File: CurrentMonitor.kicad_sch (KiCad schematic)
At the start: 33 parts, among them J1 USB_B_Micro, J10 Screw_Terminal_01x02, J11 Barrel_Jack_Switch_SMT, J12 Conn_01x05, J13 Conn_01x05, J14 USB_A, J15 Conn_Coaxial, J2 Conn_01x05, J3 Conn_01x05, J4 Barrel_Jack_Switch_SMT, J5 Screw_Terminal_01x02, J6 Conn_01x02_Socket, J7 Screw_Terminal_01x02, J8 Conn_02x03_Odd_Even, J9 Conn_01x02_Socket

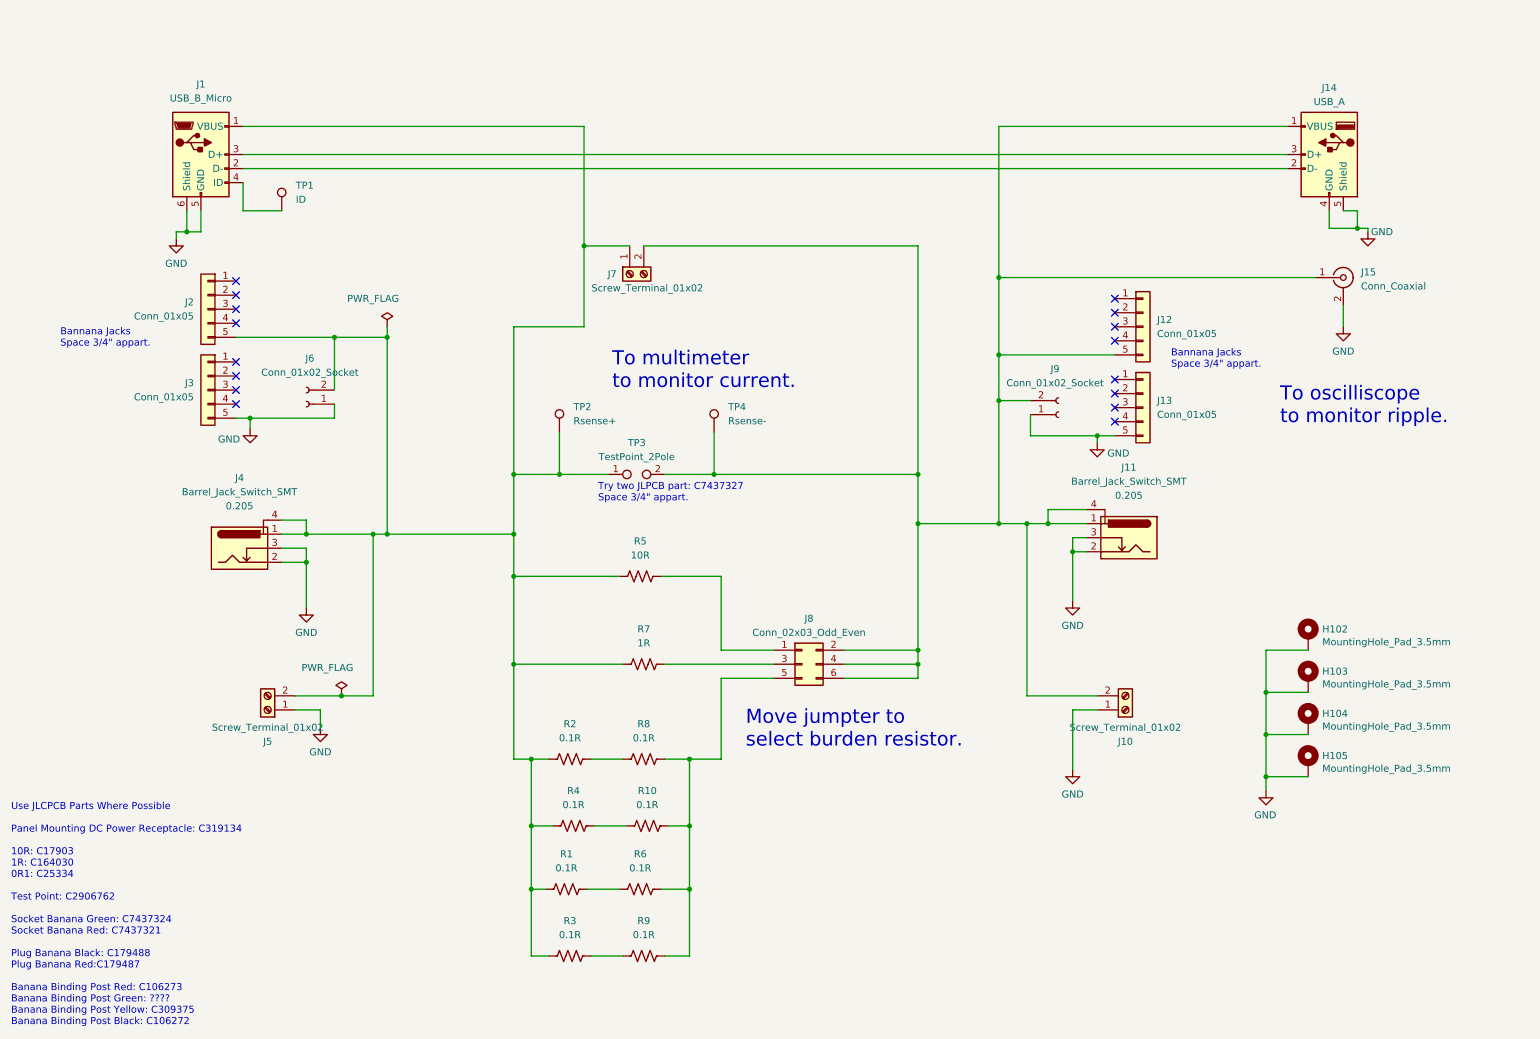
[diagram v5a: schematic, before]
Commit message: Update with USB type A footprint. Update footprint of Barrel jack, mounting holes and bannana jacks. No ERC errors.
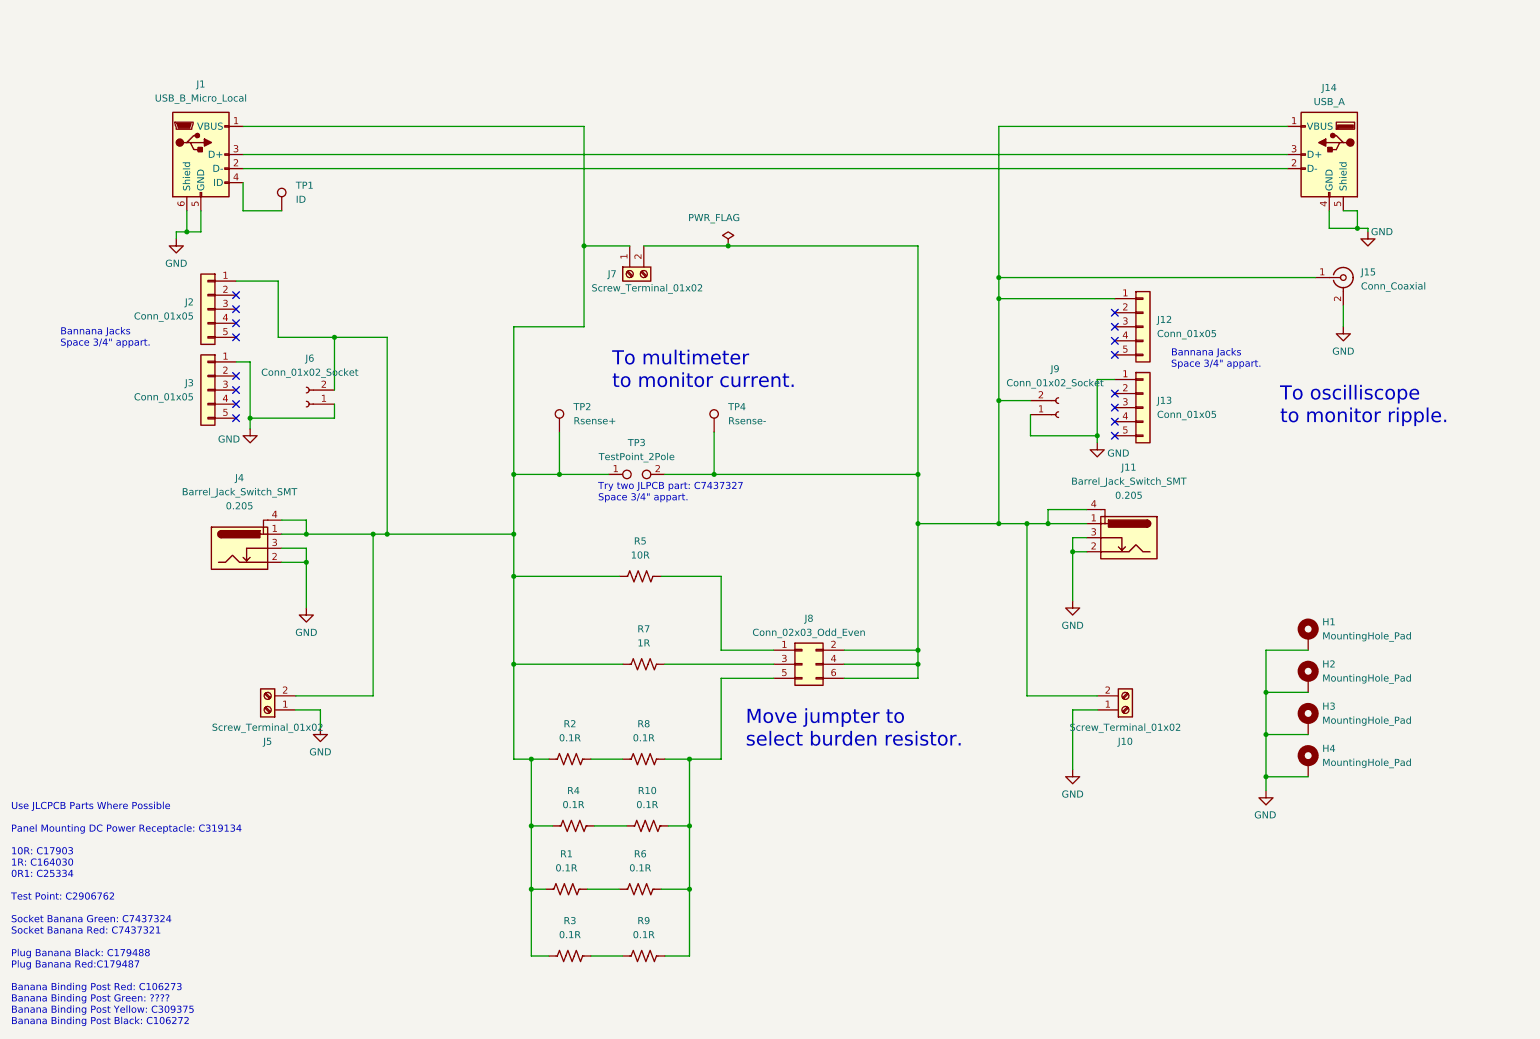
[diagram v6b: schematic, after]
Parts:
- removed H102, H103, H104, H105: MountingHole_Pad_3.5mm, MountingHole:MountingHole_3.5mm_Pad_Via, symbol GPAD_SCH_LIB:MountingHole_Pad_3.5mm
- added H1, H2, H3, H4: MountingHole_Pad, MountingHole:MountingHole_3.5mm_Pad_Via, symbol Mechanical:MountingHole_Pad
- J1: value USB_B_Micro -> USB_B_Micro_Local; footprint (none) -> PubInv_KiCad_PCB:USB_Micro-B_Amphenol_10118194_Horizontal; Cost 0.0329 -> 0.2042; Distributor 1 PN C404969 -> C132563
- J11, J4: footprint Connector_BarrelJack:BarrelJack_CLIFF_FC681465S_SMT_Horizontal -> PubInv_KiCad_PCB:BarrelJack_CLIFF_FC681465S_SMT_Horizontal
- J12, J13, J2, J3: footprint Connector:Banana_Cliff_FCR7350x_S16N-PC_Horizontal -> PubInv_KiCad_PCB:Banana_Cliff_FCR7350x_S16N-PC_Horizontal_5Pins
- J14: footprint (none) -> PubInv_KiCad_PCB:USB_A_JLCPCB_C3038692_Horizontal
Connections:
- net GND: now also J13.1 (Pin_1), J3.1 (Pin_1), H1.1, H2.1, H3.1, H4.1; no longer J13.5 (Pin_5), J3.5 (Pin_5)
- net at J1.1 (VBUS), J4.1, J4.4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: now also J2.1 (Pin_1); no longer J2.5 (Pin_5)
- net at J10.2 (Pin_2), J11.1, J11.4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: now also J12.1 (Pin_1); no longer J12.5 (Pin_5)

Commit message: Route copper on PCB.
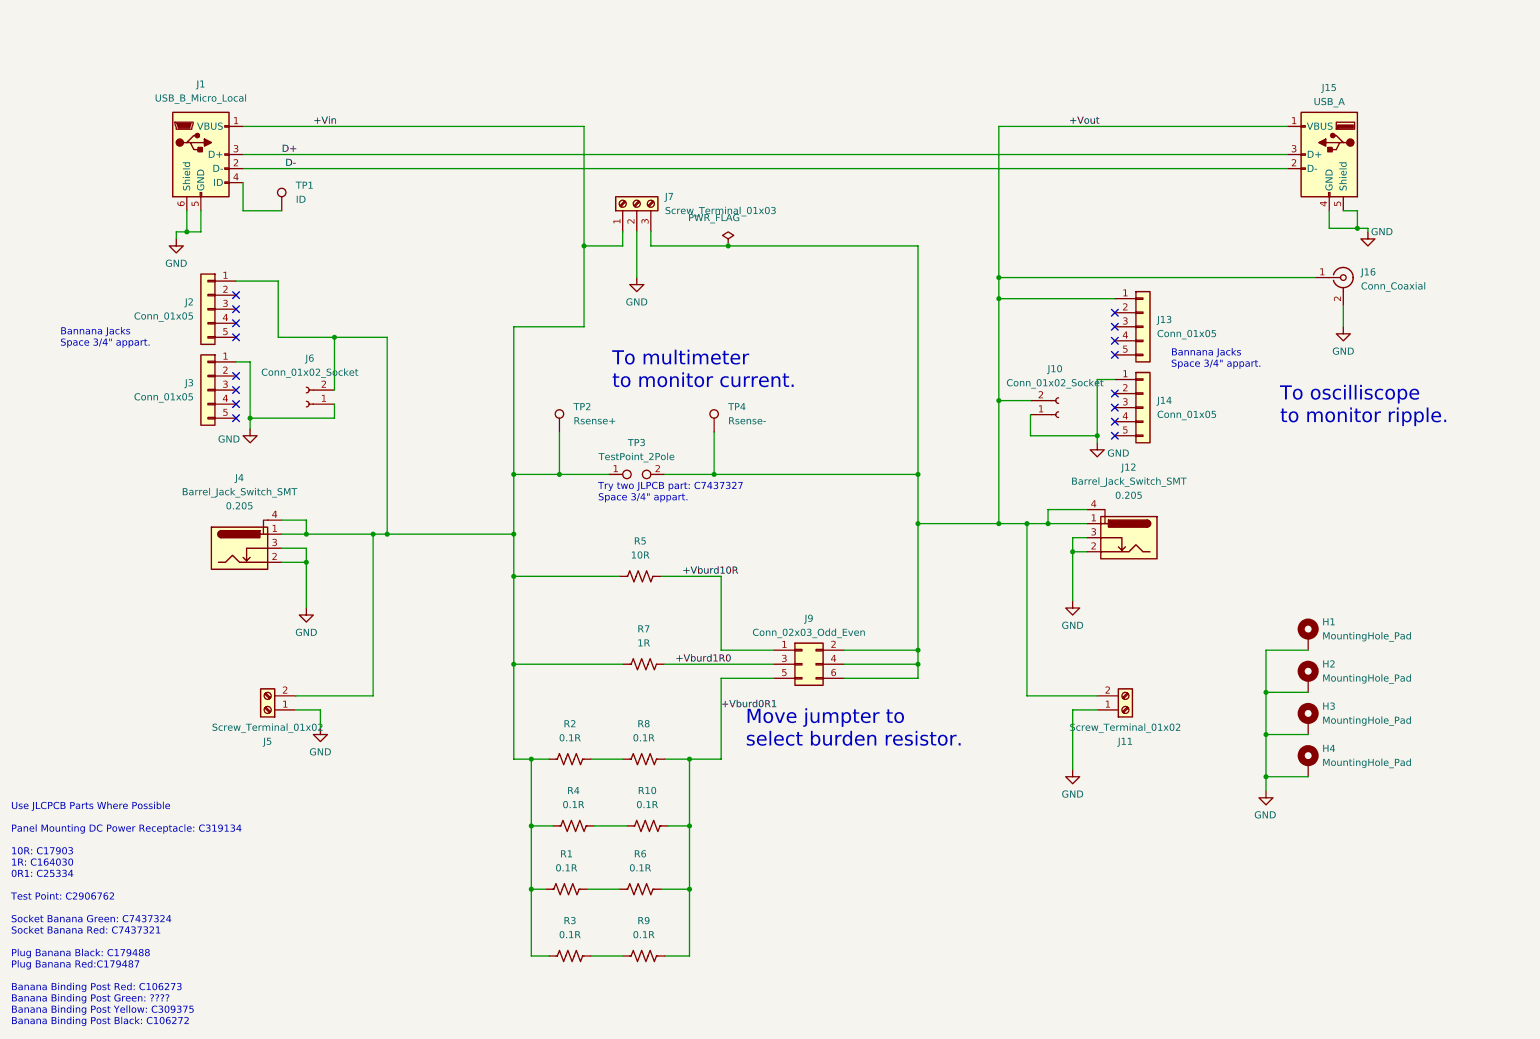
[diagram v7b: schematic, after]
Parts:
- removed J7: Screw_Terminal_01x02, TerminalBlock_Phoenix_MKDS-1,5-2_1x02_P5.00mm_Horizontal, symbol Connector:Screw_Terminal_01x02
- added J7: Screw_Terminal_01x03, TerminalBlock_Phoenix:TerminalBlock_Phoenix_MKDS-1,5-3_1x03_P5.00mm_Horizontal, symbol Connector:Screw_Terminal_01x03
- renumbered J9 to J10, J10 to J11, J11 to J12, J12 to J13, J13 to J14, J14 to J15, J15 to J16, J8 to J9
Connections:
- net GND: now also J7.2 (Pin_2)
- net +Vburd0R1: now reaches J9.5 (Pin_5), R10.2, R6.2, R8.2, R9.2
- net +Vin: now reaches J1.1 (VBUS), J2.1 (Pin_1), J4.1, J4.4, J5.2 (Pin_2), J6.2 (Pin_2), R1.1, R2.1, R3.1, R4.1, R5.1, R7.1, TP2.1, TP3.1
- net +Vin: now also J7.1 (Pin_1)
- net +Vburd1R0: now reaches J9.3 (Pin_3), R7.2
- net D-: now reaches J1.2 (D-), J15.2 (D-)
- net D+: now reaches J1.3 (D+), J15.3 (D+)
- net +Vburd10R: now reaches J9.1 (Pin_1), R5.2
- net +Vout: now reaches J10.2 (Pin_2), J11.2 (Pin_2), J12.1, J12.4, J13.1 (Pin_1), J15.1 (VBUS), J16.1 (In), J9.2 (Pin_2), J9.4 (Pin_4), J9.6 (Pin_6), TP3.2, TP4.1
- net +Vout: now also J7.3 (Pin_3)
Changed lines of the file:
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@@
+    (stroke (width 0) (type default))
+  )
+  (wire (pts (xy 130.81 52.07) (xy 130.81 60.325))
     (stroke (width 0) (type default))
   )
@@
     (stroke (width 0) (type default))
   )
+  (wire (pts (xy 133.35 52.07) (xy 133.35 54.61))
+    (stroke (width 0) (type default))
+  )
   (wire (pts (xy 60.96 75.565) (xy 60.96 85.725))
     (stroke (width 0) (type default))
@@
     (stroke (width 0) (type default))
   )
+  (wire (pts (xy 133.35 54.61) (xy 147.32 54.61))
+    (stroke (width 0) (type default))
+  )
   (wire (pts (xy 108.585 106.68) (xy 108.585 114.3))
     (stroke (width 0) (type default))
@@
     (stroke (width 0) (type default))
   )
-  (wire (pts (xy 129.54 54.61) (xy 121.285 54.61))
-    (stroke (width 0) (type default))
-  )
   (wire (pts (xy 209.55 107.315) (xy 209.55 109.855))
     (stroke (width 0) (type default))
@@
     (stroke (width 0) (type default))
   )
+  (wire (pts (xy 128.27 52.07) (xy 128.27 54.61))
+    (stroke (width 0) (type default))
+  )
   (wire (pts (xy 69.215 135.89) (xy 83.185 135.89))
     (stroke (width 0) (type default))
@@
     (stroke (width 0) (type default))
   )
+  (wire (pts (xy 128.27 54.61) (xy 121.285 54.61))
+    (stroke (width 0) (type default))
+  )
   (wire (pts (xy 196.215 82.55) (xy 201.93 82.55))
     (stroke (width 0) (type default))
@@
   )
   (wire (pts (xy 116.84 95.885) (xy 108.585 95.885))
-    (stroke (width 0) (type default))
-  )
-  (wire (pts (xy 132.08 54.61) (xy 147.32 54.61))
     (stroke (width 0) (type default))
   )
@@
   )
   (text "Bannana Jacks\nSpace 3/4\" appart." (at 227.33 76.835 0)
+    (effects (font (size 1.27 1.27)) (justify left bottom))
+  )
+  (label "D-" (at 67.31 40.64 0) (fields_autoplaced)
+    (effects (font (size 1.27 1.27)) (justify left bottom))
+  )
+  (label "+Vout" (at 208.915 33.02 0) (fields_autoplaced)
+    (effects (font (size 1.27 1.27)) (justify left bottom))
+  )
+  (label "+Vburd10R" (at 139.065 114.3 0) (fields_autoplaced)
+    (effects (font (size 1.27 1.27)) (justify left bottom))
+  )
+  (label "+Vin" (at 72.39 33.02 0) (fields_autoplaced)
+    (effects (font (size 1.27 1.27)) (justify left bottom))
+  )
+  (label "+Vburd1R0" (at 137.795 130.175 0) (fields_autoplaced)
+    (effects (font (size 1.27 1.27)) (justify left bottom))
+  )
+  (label "+Vburd0R1" (at 146.05 138.43 0) (fields_autoplaced)
+    (effects (font (size 1.27 1.27)) (justify left bottom))
+  )
+  (label "D+" (at 66.675 38.1 0) (fields_autoplaced)
     (effects (font (size 1.27 1.27)) (justify left bottom))
   )
@@
   (symbol (lib_id "Connector:USB_A") (at 255.905 38.1 0) (mirror y) (unit 1)
     (in_bom yes) (on_board yes) (dnp no)
-    (property "Reference" "J14" (at 255.905 26.035 0)
+    (property "Reference" "J15" (at 255.905 26.035 0)
       (effects (font (size 1.27 1.27)))
     )
@@
       (project "CurrentMonitor"
         (path "/c2625580-5dc2-4487-938a-c703153fa89f"
-          (reference "J14") (unit 1)
+          (reference "J15") (unit 1)
         )
       )
@@
   (symbol (lib_id "Connector_Generic:Conn_02x03_Odd_Even") (at 160.655 130.175 0) (unit 1)
     (in_bom yes) (on_board yes) (dnp no) (fields_autoplaced)
-    (property "Reference" "J8" (at 161.925 121.92 0)
+    (property "Reference" "J9" (at 161.925 121.92 0)
       (effects (font (size 1.27 1.27)))
     )
@@
       (project "CurrentMonitor"
         (path "/c2625580-5dc2-4487-938a-c703153fa89f"
-          (reference "J8") (unit 1)
+          (reference "J9") (unit 1)
         )
       )
@@
   (symbol (lib_id "Connector:Screw_Terminal_01x02") (at 219.075 138.43 0) (mirror x) (unit 1)
     (in_bom yes) (on_board yes) (dnp no)
-    (property "Reference" "J10" (at 219.075 144.145 0)
+    (property "Reference" "J11" (at 219.075 144.145 0)
       (effects (font (size 1.27 1.27)))
     )
@@
       (project "CurrentMonitor"
         (path "/c2625580-5dc2-4487-938a-c703153fa89f"
-          (reference "J10") (unit 1)
+          (reference "J11") (unit 1)
         )
       )
@@
   (symbol (lib_id "Connector_Generic:Conn_01x05") (at 222.25 69.215 0) (unit 1)
     (in_bom yes) (on_board yes) (dnp no) (fields_autoplaced)
-    (property "Reference" "J12" (at 224.79 67.945 0)
+    (property "Reference" "J13" (at 224.79 67.945 0)
       (effects (font (size 1.27 1.27)) (justify left))
     )
@@
       (project "CurrentMonitor"
         (path "/c2625580-5dc2-4487-938a-c703153fa89f"
-          (reference "J12") (unit 1)
+          (reference "J13") (unit 1)
         )
       )
@@
   (symbol (lib_id "PubInv_KiCad_SCH_LIB:Barrel_Jack_Switch_SMT") (at 219.71 107.315 0) (mirror y) (unit 1)
     (in_bom yes) (on_board yes) (dnp no)
-    (property "Reference" "J11" (at 219.71 94.615 0)
+    (property "Reference" "J12" (at 219.71 94.615 0)
       (effects (font (size 1.27 1.27)))
     )
@@
       (project "CurrentMonitor"
         (path "/c2625580-5dc2-4487-938a-c703153fa89f"
-          (reference "J11") (unit 1)
+          (reference "J12") (unit 1)
         )
       )
@@
   (symbol (lib_id "Connector:Conn_01x02_Socket") (at 207.01 85.09 0) (mirror x) (unit 1)
     (in_bom no) (on_board yes) (dnp no)
-    (property "Reference" "J9" (at 206.375 76.835 0)
+    (property "Reference" "J10" (at 206.375 76.835 0)
       (effects (font (size 1.27 1.27)))
     )
@@
       (project "CurrentMonitor"
         (path "/c2625580-5dc2-4487-938a-c703153fa89f"
-          (reference "J9") (unit 1)
-        )
-      )
-    )
-  )
-  (symbol (lib_id "Connector:Screw_Terminal_01x02") (at 129.54 59.69 90) (mirror x) (unit 1)
-    (in_bom yes) (on_board yes) (dnp no)
-    (property "Reference" "J7" (at 126.365 59.69 90)
-      (effects (font (size 1.27 1.27)))
-    )
-    (property "Value" "Screw_Terminal_01x02" (at 132.715 62.23 90)
-      (effects (font (size 1.27 1.27)))
-    )
-    (property "Footprint" "TerminalBlock_Phoenix_MKDS-1,5-2_1x02_P5.00mm_Horizontal" (at 129.54 59.69 0)
-      (effects (font (size 1.27 1.27)) hide)
-    )
-    (property "Datasheet" "~" (at 129.54 59.69 0)
-      (effects (font (size 1.27 1.27)) hide)
-    )
-    (property "Distributor 1" "JLCPCB" (at 129.54 59.69 0)
-      (effects (font (size 1.27 1.27)) hide)
-    )
-    (property "Distributor 1 PN" "C8385" (at 129.54 59.69 0)
-      (effects (font (size 1.27 1.27)) hide)
-    )
-    (property "Description" "1x2P -30℃~+120℃ 17.5A 250V Blue 14~22 Straight 5mm 1.5 1 2 Plugin,P=5mm Screw terminal ROHS" (at 129.54 59.69 0)
-      (effects (font (size 1.27 1.27)) hide)
-    )
-    (property "Cost" "0.0764" (at 129.54 59.69 0)
-      (effects (font (size 1.27 1.27)) hide)
-    )
-    (pin "1")
-    (pin "2")
-    (instances
-      (project "CurrentMonitor"
-        (path "/c2625580-5dc2-4487-938a-c703153fa89f"
-          (reference "J7") (unit 1)
+          (reference "J10") (unit 1)
         )
       )
@@
   (symbol (lib_id "Connector:Conn_Coaxial") (at 258.445 60.325 0) (unit 1)
     (in_bom yes) (on_board yes) (dnp no) (fields_autoplaced)
-    (property "Reference" "J15" (at 261.62 59.3482 0)
+    (property "Reference" "J16" (at 261.62 59.3482 0)
       (effects (font (size 1.27 1.27)) (justify left))
     )
@@
       (project "CurrentMonitor"
         (path "/c2625580-5dc2-4487-938a-c703153fa89f"
-          (reference "J15") (unit 1)
+          (reference "J16") (unit 1)
         )
       )
@@
     )
   )
+  (symbol (lib_id "Connector:Screw_Terminal_01x03") (at 130.81 46.99 90) (unit 1)
+    (in_bom yes) (on_board yes) (dnp no) (fields_autoplaced)
+    (property "Reference" "J7" (at 135.89 45.72 90)
+      (effects (font (size 1.27 1.27)) (justify right))
+    )
+    (property "Value" "Screw_Terminal_01x03" (at 135.89 48.26 90)
+      (effects (font (size 1.27 1.27)) (justify right))
+    )
+    (property "Footprint" "TerminalBlock_Phoenix:TerminalBlock_Phoenix_MKDS-1,5-3_1x03_P5.00mm_Horizontal" (at 130.81 46.99 0)
+      (effects (font (size 1.27 1.27)) hide)
+    )
+    (property "Datasheet" "~" (at 130.81 46.99 0)
+      (effects (font (size 1.27 1.27)) hide)
+    )
+    (property "Description" "1x3P -30℃~+120℃ 17.5A 250V Blue 14~22 Straight 5mm 1.5 1 3 Plugin,P=5mm Screw terminal ROHS" (at 130.81 46.99 0)
+      (effects (font (size 1.27 1.27)) hide)
+    )
+    (property "Distributor 1" "JLCPCB" (at 130.81 46.99 0)
+      (effects (font (size 1.27 1.27)) hide)
+    )
+    (property "Distributor 1 PN" "C8467" (at 130.81 46.99 0)
+      (effects (font (size 1.27 1.27)) hide)
+    )
+    (pin "1")
+    (pin "2")
+    (pin "3")
+    (instances
+      (project "CurrentMonitor"
+        (path "/c2625580-5dc2-4487-938a-c703153fa89f"
+          (reference "J7") (unit 1)
+        )
+      )
+    )
+  )
   (symbol (lib_id "Connector_Generic:Conn_01x05") (at 222.25 83.82 0) (unit 1)
     (in_bom yes) (on_board yes) (dnp no) (fields_autoplaced)
-    (property "Reference" "J13" (at 224.79 82.55 0)
+    (property "Reference" "J14" (at 224.79 82.55 0)
       (effects (font (size 1.27 1.27)) (justify left))
     )
@@
       (project "CurrentMonitor"
         (path "/c2625580-5dc2-4487-938a-c703153fa89f"
-          (reference "J13") (unit 1)
+          (reference "J14") (unit 1)
         )
       )
@@
         )
       )
+    )
+  )
+  (symbol (lib_id "power:GND") (at 130.81 60.325 0) (unit 1)
+    (in_bom yes) (on_board yes) (dnp no) (fields_autoplaced)
+    (property "Reference" "#PWR011" (at 130.81 66.675 0)
+      (effects (font (size 1.27 1.27)) hide)
+    )
+    (property "Value" "GND" (at 130.81 64.77 0)
+      (effects (font (size 1.27 1.27)))
+    )
+    (property "Footprint" "" (at 130.81 60.325 0)
+      (effects (font (size 1.27 1.27)) hide)
+    )
+    (property "Datasheet" "" (at 130.81 60.325 0)
+      (effects (font (size 1.27 1.27)) hide)
+    )
+    (pin "1")
+    (instances
+      (project "CurrentMonitor"
+        (path "/c2625580-5dc2-4487-938a-c703153fa89f"
+          (reference "#PWR011") (unit 1)
+        )
+      )
